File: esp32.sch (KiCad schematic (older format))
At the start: 11 parts, among them U24 ESP32-PICO-D4

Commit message: Route ESP32 SPI bus
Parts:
- added C?: 10uF, Capacitor_SMD:C_0402_1005Metric, symbol Device:C_Small
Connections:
- net 3V3: now also C?.2
- net GND: now also C?.1
- net VSPICLK renamed CLK
- net VSPICS renamed ~CS
- net VSPID renamed MOSI
- net VSPIQ renamed MISO
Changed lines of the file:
@@
 	5900 1350 5900 1600
 Connection ~ 5900 1600
-Text HLabel 2900 1500 0    50   Input ~ 0
+Text HLabel 2550 1500 0    50   Input ~ 0
 3V3
 Connection ~ 3650 1500
@@
 Wire Wire Line
 	3300 1500 3650 1500
-Wire Wire Line
-	2900 1500 2950 1500
 Connection ~ 2950 1500
 Text Label 6200 2850 2    50   ~ 0
@@
 Text Label 6200 3450 2    50   ~ 0
 HSPICS
+Text HLabel 6200 3550 2    50   Output ~ 0
+CLK
+Text HLabel 6200 2850 2    50   Output ~ 0
+~CS
+Text HLabel 6200 3950 2    50   Output ~ 0
+MOSI
+Text HLabel 6200 3650 2    50   Input ~ 0
+MISO
+$Comp
+L Device:C_Small C?
+U 1 1 6223E7DE
+P 2600 1650
+F 0 "C?" H 2508 1604 50  0000 R CNN
+F 1 "10uF" H 2508 1695 50  0000 R CNN
+F 2 "Capacitor_SMD:C_0402_1005Metric" H 2600 1650 50  0001 C CNN
+F 3 "~" H 2600 1650 50  0001 C CNN
+F 4 "C15525" H 2600 1650 50  0001 C CNN "LCSC"
+	1    2600 1650
+	-1   0    0    1
+$EndComp
+Wire Wire Line
+	2550 1500 2600 1500
+Wire Wire Line
+	2600 1550 2600 1500
+Connection ~ 2600 1500
+Wire Wire Line
+	2600 1500 2950 1500
+Wire Wire Line
+	2950 1750 2600 1750
+Connection ~ 2950 1750
 $EndSCHEMATC

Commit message: Add preliminary ESP32 power layout
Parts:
- added C?: 100nF, Capacitor_SMD:C_0402_1005Metric, symbol Device:C_Small
- added R?: 100k, Resistor_SMD:R_0402_1005Metric, symbol Device:R_Small
- gave numbers to parts that had none: 1
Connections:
- net 3V3: now also R?.2
- net EN: now also C?.1, R?.1
- net GND: now also C?.2
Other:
- moved on the sheet: C21, C22, C23, C24, C28, C29, C39

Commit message: Layout horizontal busses
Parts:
- gave numbers to parts that had none: 2
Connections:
- net SCL: now reaches U24.39 (IO22)
- net SDA: now reaches U24.42 (IO21)
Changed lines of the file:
@@
 U 1 1 62268FD1
 P 4050 2000
-F 0 "R?" H 3992 1954 50  0000 R CNN
+AR Path="/62268FD1" Ref="R?"  Part="1"
+AR Path="/620161BA/62268FD1" Ref="R6"  Part="1"
+F 0 "R6" H 3992 1954 50  0000 R CNN
 F 1 "100k" H 3992 2045 50  0000 R CNN
 F 2 "Resistor_SMD:R_0402_1005Metric" H 4050 2000 50  0001 C CNN
@@
 AR Path="/61C4C905/61A75B93/62268FD8" Ref="C?"  Part="1"
 AR Path="/62268FD8" Ref="C?"  Part="1"
-F 0 "C?" V 3821 2300 50  0000 C CNN
+AR Path="/620161BA/62268FD8" Ref="C40"  Part="1"
+F 0 "C40" V 3821 2300 50  0000 C CNN
 F 1 "100nF" V 3912 2300 50  0000 C CNN
 F 2 "Capacitor_SMD:C_0402_1005Metric" H 4050 2300 50  0001 C CNN
@@
 	4050 2150 4250 2150
 $Comp
-L power:GND #PWR?
+L power:GND #PWR0181
 U 1 1 6226FEA7
 P 4050 2450
-F 0 "#PWR?" H 4050 2200 50  0001 C CNN
+F 0 "#PWR0181" H 4050 2200 50  0001 C CNN
 F 1 "GND" H 4055 2277 50  0000 C CNN
 F 2 "" H 4050 2450 50  0001 C CNN
@@
 Wire Wire Line
 	4050 1500 3950 1500
+Wire Wire Line
+	5850 3750 6200 3750
+Text Label 6200 3750 2    50   ~ 0
+SDA
+Wire Wire Line
+	5850 3850 6200 3850
+Text Label 6200 3850 2    50   ~ 0
+SCL
+Text HLabel 6200 3850 2    50   Output ~ 0
+SCL
+Text HLabel 6200 3750 2    50   BiDi ~ 0
+SDA
 $EndSCHEMATC

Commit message: Implement power path
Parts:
- added R13, R14: 5.1k, Resistor_SMD:R_0402_1005Metric, symbol Device:R_Small
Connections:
- net 3V3: now also R13.1, R14.1
- net SCL: now also R14.2
- net SDA: now also R13.2
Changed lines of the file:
@@
 Wire Wire Line
 	4050 1500 3950 1500
-Wire Wire Line
-	5850 3750 6200 3750
 Text Label 6200 3750 2    50   ~ 0
 SDA
-Wire Wire Line
-	5850 3850 6200 3850
 Text Label 6200 3850 2    50   ~ 0
 SCL
-Text HLabel 6200 3850 2    50   Output ~ 0
+Text HLabel 6800 3850 2    50   Output ~ 0
 SCL
-Text HLabel 6200 3750 2    50   BiDi ~ 0
+Text HLabel 6800 3750 2    50   BiDi ~ 0
 SDA
+Text HLabel 6250 4300 2    50   Input ~ 0
+IRQ
+$Comp
+L Device:R_Small R?
+U 1 1 629BE50E
+P 6500 3550
+AR Path="/629BE50E" Ref="R?"  Part="1"
+AR Path="/620161BA/629BE50E" Ref="R13"  Part="1"
+F 0 "R13" V 6400 3700 50  0000 C CNN
+F 1 "5.1k" V 6400 3500 50  0000 C CNN
+F 2 "Resistor_SMD:R_0402_1005Metric" H 6500 3550 50  0001 C CNN
+F 3 "~" H 6500 3550 50  0001 C CNN
+F 4 "C23186" H 6500 3550 50  0001 C CNN "LCSC"
+	1    6500 3550
+	-1   0    0    -1
+$EndComp
+Wire Wire Line
+	5850 3750 6500 3750
+Wire Wire Line
+	5850 3850 6700 3850
+$Comp
+L Device:R_Small R?
+U 1 1 629C2CA3
+P 6700 3550
+AR Path="/629C2CA3" Ref="R?"  Part="1"
+AR Path="/620161BA/629C2CA3" Ref="R14"  Part="1"
+F 0 "R14" V 6600 3700 50  0000 C CNN
+F 1 "5.1k" V 6600 3500 50  0000 C CNN
+F 2 "Resistor_SMD:R_0402_1005Metric" H 6700 3550 50  0001 C CNN
+F 3 "~" H 6700 3550 50  0001 C CNN
+F 4 "C23186" H 6700 3550 50  0001 C CNN "LCSC"
+	1    6700 3550
+	-1   0    0    -1
+$EndComp
+Wire Wire Line
+	6700 3650 6700 3850
+Connection ~ 6700 3850
+Wire Wire Line
+	6700 3850 6800 3850
+Wire Wire Line
+	6500 3650 6500 3750
+Connection ~ 6500 3750
+Wire Wire Line
+	6500 3750 6800 3750
+Text Label 4850 1500 0    50   ~ 0
+3V3
+Wire Wire Line
+	6500 3450 6500 3350
+Wire Wire Line
+	6500 3350 6700 3350
+Wire Wire Line
+	6700 3350 6700 3450
+Text Label 6500 3350 0    50   ~ 0
+3V3
 $EndSCHEMATC

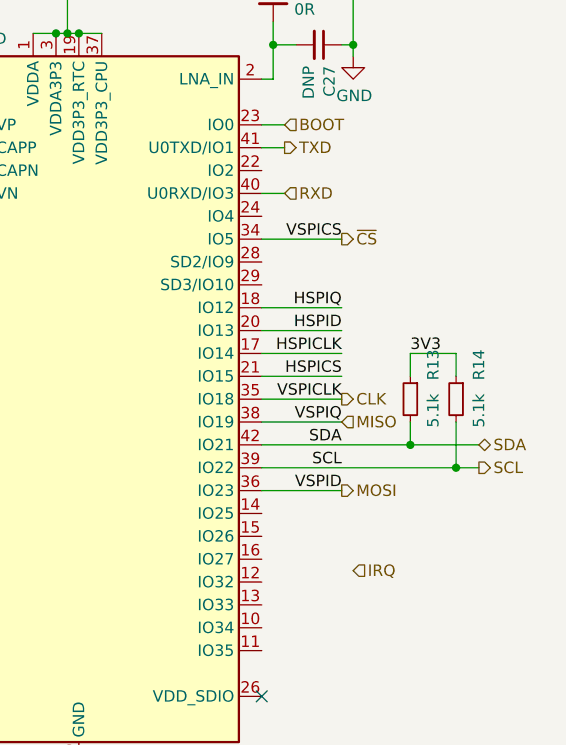
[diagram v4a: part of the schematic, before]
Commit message: Layout remaining busses
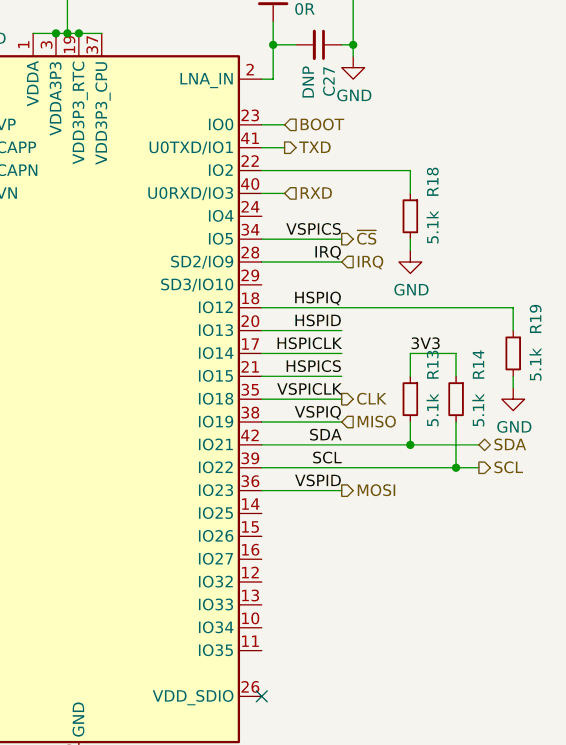
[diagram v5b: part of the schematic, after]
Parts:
- added R18, R19: 5.1k, Resistor_SMD:R_0402_1005Metric, symbol Device:R_Small
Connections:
- net GND: now also R18.2, R19.2
- net HSPIQ: now also R19.1
- net IRQ: now also U24.28 (SD2/IO9)
- net at U24.22 (IO2): now also R18.1
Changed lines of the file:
@@
 Text Label 6200 3350 2    50   ~ 0
 HSPICLK
-Wire Wire Line
-	5850 3150 6200 3150
 Text Label 6200 3150 2    50   ~ 0
 HSPIQ
@@
 Text HLabel 6800 3750 2    50   BiDi ~ 0
 SDA
-Text HLabel 6250 4300 2    50   Input ~ 0
+Text HLabel 6200 2950 2    50   Input ~ 0
 IRQ
 $Comp
@@
 Text Label 6500 3350 0    50   ~ 0
 3V3
+$Comp
+L Device:R_Small R?
+U 1 1 62E05746
+P 6500 2750
+AR Path="/62E05746" Ref="R?"  Part="1"
+AR Path="/620161BA/62E05746" Ref="R18"  Part="1"
+F 0 "R18" V 6400 2900 50  0000 C CNN
+F 1 "5.1k" V 6400 2700 50  0000 C CNN
+F 2 "Resistor_SMD:R_0402_1005Metric" H 6500 2750 50  0001 C CNN
+F 3 "~" H 6500 2750 50  0001 C CNN
+F 4 "C23186" H 6500 2750 50  0001 C CNN "LCSC"
+	1    6500 2750
+	-1   0    0    -1
+$EndComp
+Wire Wire Line
+	5850 2550 6500 2550
+Wire Wire Line
+	6500 2550 6500 2650
+$Comp
+L power:GND #PWR0201
+U 1 1 62E0842B
+P 6500 2900
+F 0 "#PWR0201" H 6500 2650 50  0001 C CNN
+F 1 "GND" H 6505 2727 50  0000 C CNN
+F 2 "" H 6500 2900 50  0001 C CNN
+F 3 "" H 6500 2900 50  0001 C CNN
+	1    6500 2900
+	1    0    0    -1
+$EndComp
+Wire Wire Line
+	6500 2900 6500 2850
+$Comp
+L Device:R_Small R?
+U 1 1 62E0AE9E
+P 6950 3350
+AR Path="/62E0AE9E" Ref="R?"  Part="1"
+AR Path="/620161BA/62E0AE9E" Ref="R19"  Part="1"
+F 0 "R19" V 6850 3500 50  0000 C CNN
+F 1 "5.1k" V 6850 3300 50  0000 C CNN
+F 2 "Resistor_SMD:R_0402_1005Metric" H 6950 3350 50  0001 C CNN
+F 3 "~" H 6950 3350 50  0001 C CNN
+F 4 "C23186" H 6950 3350 50  0001 C CNN "LCSC"
+	1    6950 3350
+	-1   0    0    -1
+$EndComp
+Wire Wire Line
+	6950 3150 6950 3250
+$Comp
+L power:GND #PWR0202
+U 1 1 62E0AEA6
+P 6950 3500
+F 0 "#PWR0202" H 6950 3250 50  0001 C CNN
+F 1 "GND" H 6955 3327 50  0000 C CNN
+F 2 "" H 6950 3500 50  0001 C CNN
+F 3 "" H 6950 3500 50  0001 C CNN
+	1    6950 3500
+	1    0    0    -1
+$EndComp
+Wire Wire Line
+	6950 3500 6950 3450
+Wire Wire Line
+	5850 3150 6950 3150
+Wire Wire Line
+	5850 2950 6200 2950
+Text Label 6200 2950 2    50   ~ 0
+IRQ
 $EndSCHEMATC

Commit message: Use better ESP32 Pico D4 footprint
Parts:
- C25: LCSC (none) -> C17168
- U24: footprint Package_DFN_QFN:QFN-48-1EP_7x7mm_P0.5mm_EP5.3x5.3mm -> Package_ESP32:ESP32-Pico-D4
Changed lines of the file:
@@
 F 0 "U24" H 5050 1861 50  0000 C CNN
 F 1 "ESP32-PICO-D4" H 5050 1770 50  0000 C CNN
-F 2 "Package_DFN_QFN:QFN-48-1EP_7x7mm_P0.5mm_EP5.3x5.3mm" H 5050 1850 50  0001 C CNN
+F 2 "Package_ESP32:ESP32-Pico-D4" H 5050 1850 50  0001 C CNN
 F 3 "https://www.espressif.com/sites/default/files/documentation/esp32-pico-d4_datasheet_en.pdf" H 5300 2550 50  0001 C CNN
 F 4 "C193707" H 5050 3550 50  0001 C CNN "LCSC"
@@
 F 2 "Capacitor_SMD:C_0402_1005Metric" H 5900 1800 50  0001 C CNN
 F 3 "~" H 5900 1800 50  0001 C CNN
+F 4 "C17168" H 5900 1800 50  0001 C CNN "LCSC"
 	1    5900 1800
 	1    0    0    -1
